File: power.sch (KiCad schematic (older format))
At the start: 57 parts, among them J201 Conn_01x02_Male, J202 T12_Sense, J203 T12_POWER, Q201 2N7002, Q202 FDS4435BZ, U201 ACS756xCB-050B-PFF, U202 TPS5430DDAR, U203 AMS1117-5.0, U204 OPA237NA_250, U205 AMS1117-3.3, U206 OPA237NA_250

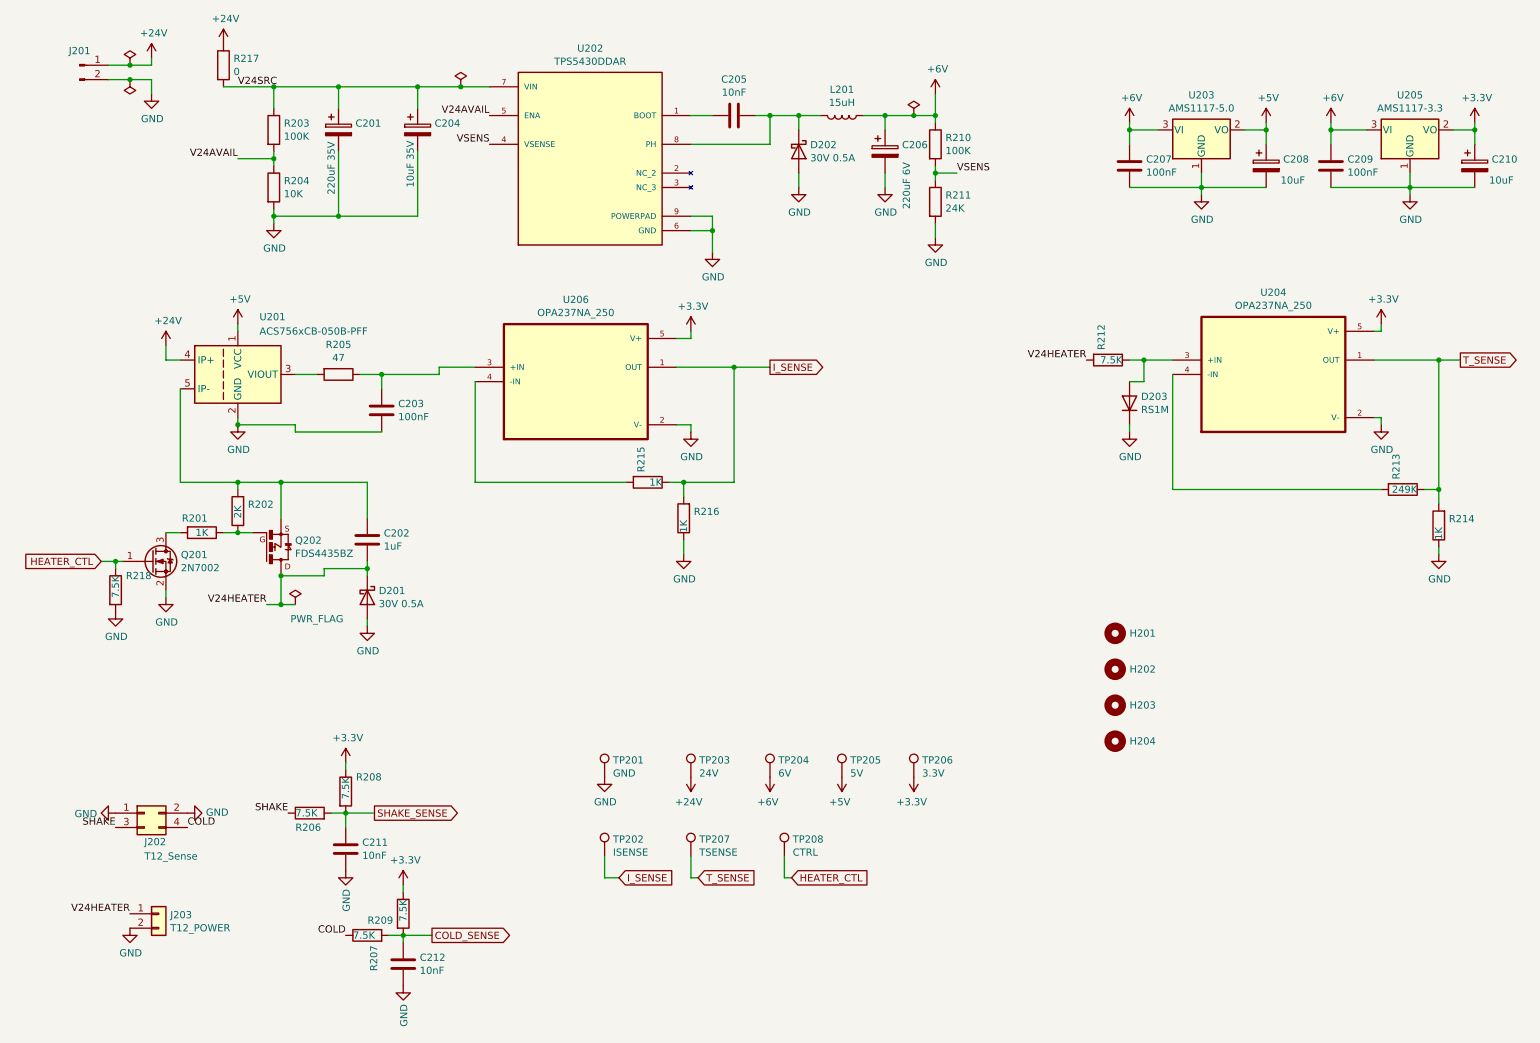
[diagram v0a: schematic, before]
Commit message: Fix ST12 schematics with current sensor (tested on balcony patch)
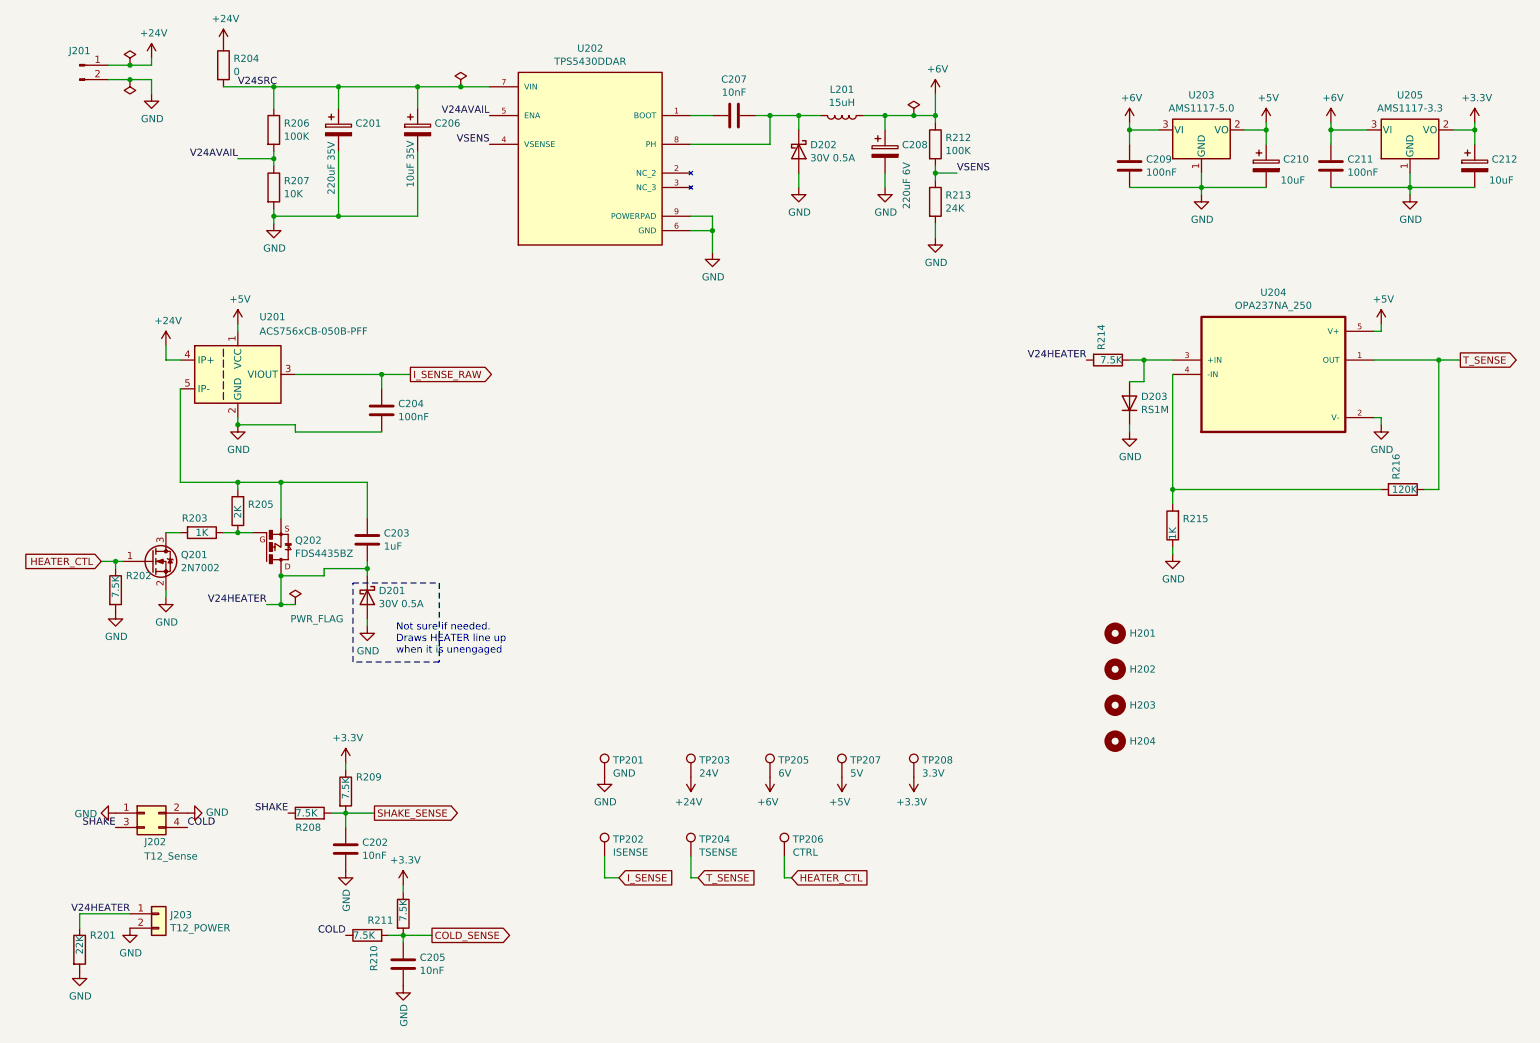
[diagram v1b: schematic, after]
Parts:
- removed R205: 47, Resistors_SMD:R_0603_HandSoldering, symbol Device:R
- removed R215, R216: 1K, Resistors_SMD:R_1206_HandSoldering, symbol Device:R
- removed U206: OPA237NA_250, OPA237NA:SOT95P280X145-5N, symbol OPA237NA_250:OPA237NA_250
- added R201: 22K, Resistors_SMD:R_0805_HandSoldering, symbol Device:R
- R216: renamed from R213; value 249K -> 120K
- renumbered C211 to C202, C202 to C203, C203 to C204, C212 to C205, C204 to C206, C205 to C207, C206 to C208, C207 to C209, C208 to C210, C209 to C211, C210 to C212, R218 to R202, R201 to R203, R217 to R204, R202 to R205, R203 to R206, R204 to R207, R206 to R208, R208 to R209, R207 to R210, R209 to R211, R210 to R212, R211 to R213, R212 to R214, R214 to R215, TP207 to TP204, TP204 to TP205, TP208 to TP206, TP205 to TP207, TP206 to TP208
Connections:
- net +3V3: no longer U204.5 (V+)
- net +5V: now also U204.5 (V+)
- net GND: now also R201.2
- net T_SENSE: no longer R215.2
- net V24HEATER: now also R201.1
- net I_SENSE_RAW: now reaches U201.3 (VIOUT)
- net I_SENSE_RAW: now also C204.1
- net at R216.2, U204.4 (-IN): now also R215.2
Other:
- note added: "Not sure if needed.\nDraws HEATER line up\nwhen it is unengaged"
- moved on the sheet: R215
